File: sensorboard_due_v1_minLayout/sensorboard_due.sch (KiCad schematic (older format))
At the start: 35 parts, among them J1 LED_PANEL, J10 DHT22, J11 DHT2_JUMP, J12 DHT4_JUMP, J13 DHT22, J14 DHT22, J2 I2C_SLAVE, J3 WATCHDOG, J4 GPS_UBLOX_NEO6M, J5 GPS_DIS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

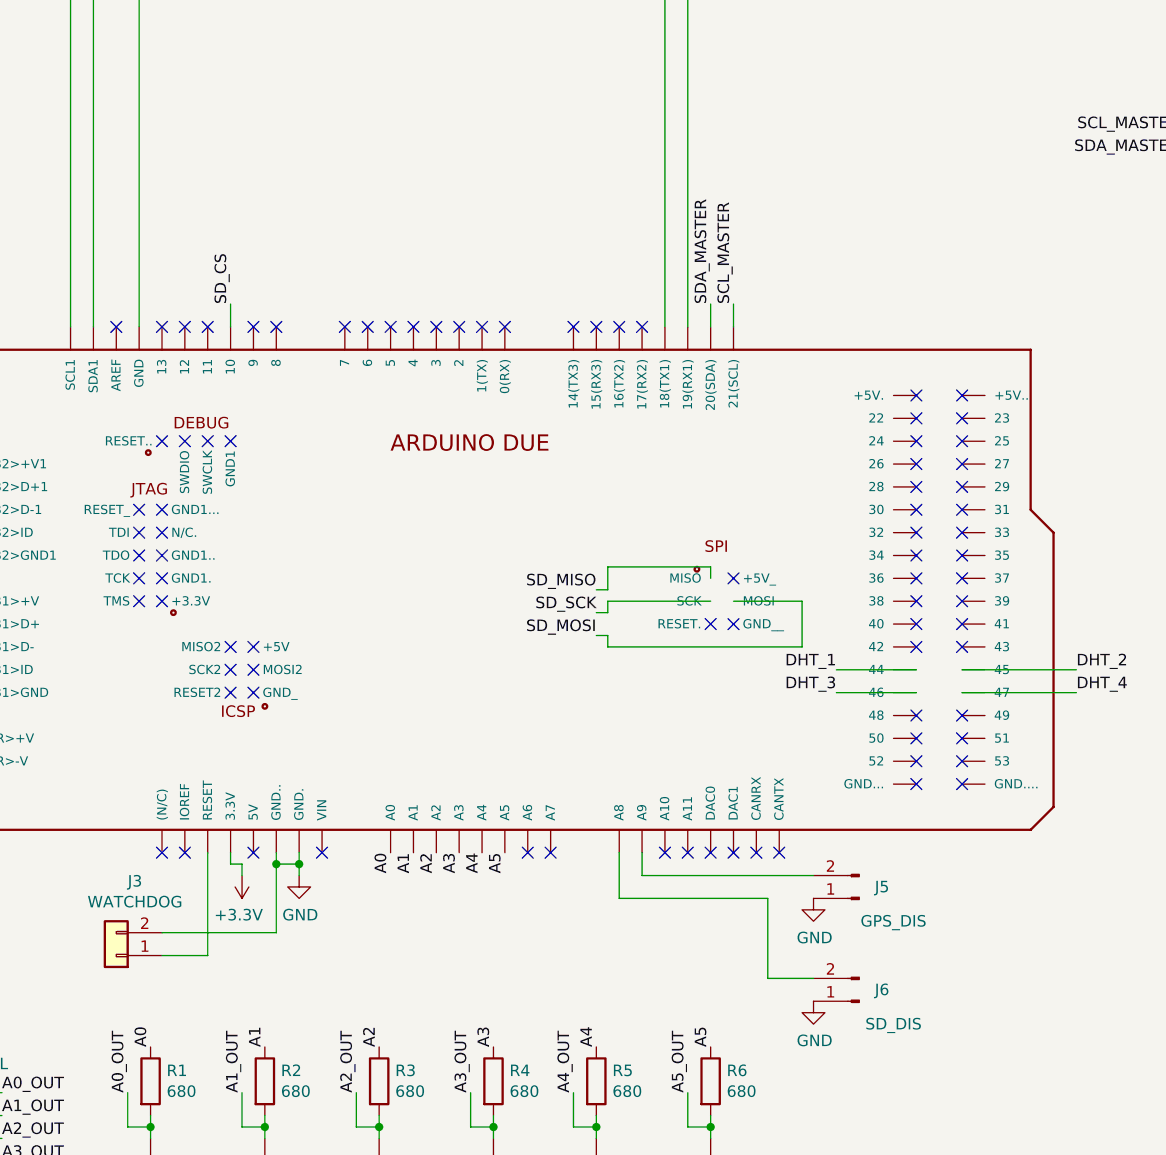
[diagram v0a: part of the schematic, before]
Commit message: pcb footprints for breadboard components should be accurate to datasheet (callipers if no ds) now
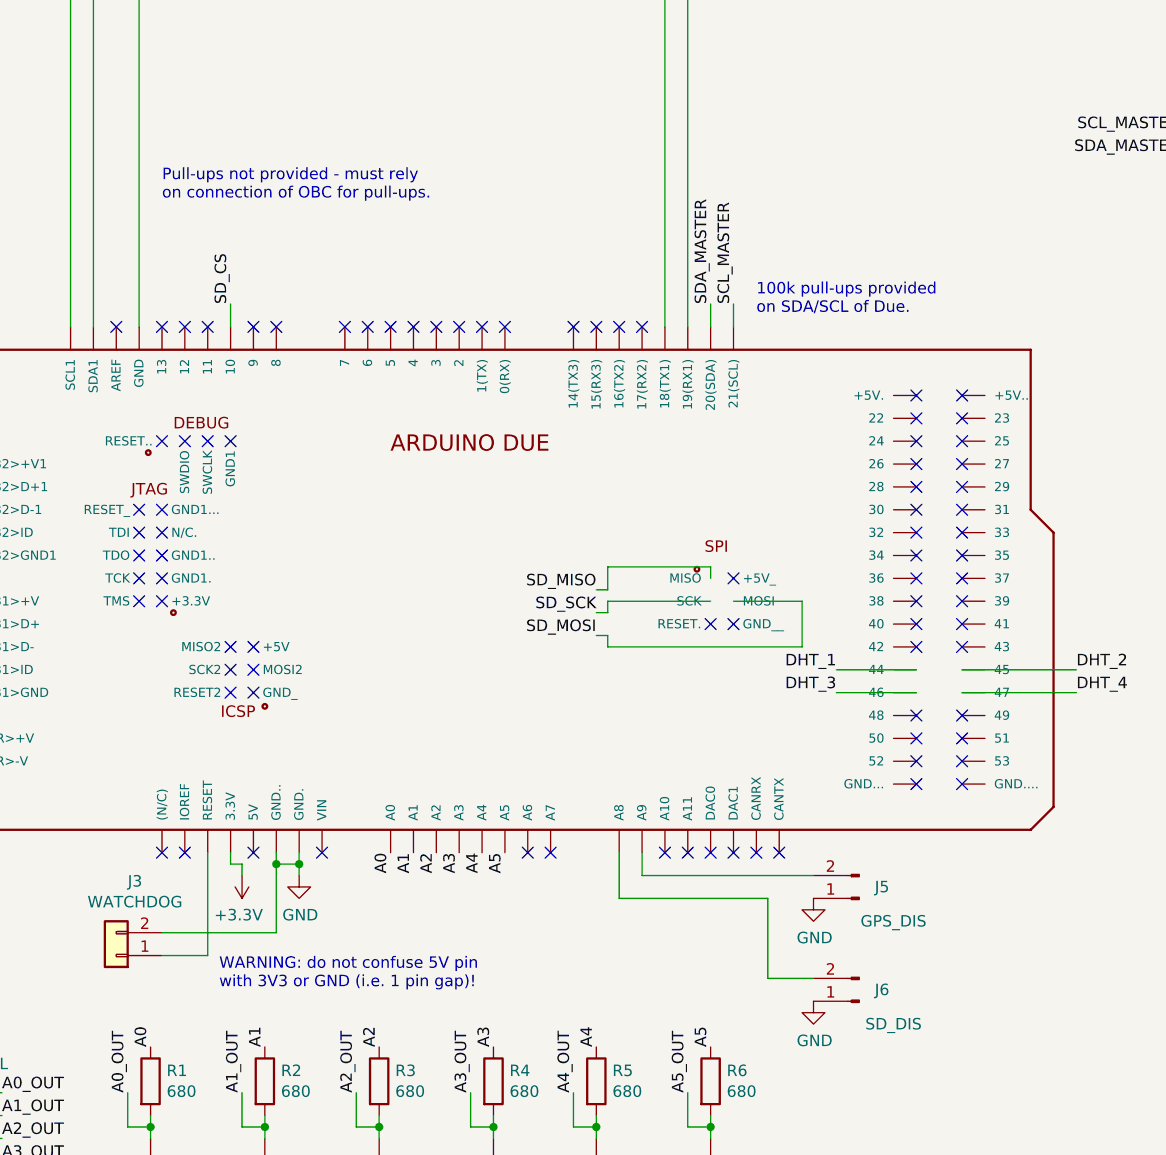
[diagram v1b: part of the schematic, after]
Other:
- note added: "100k pull-ups provided\non SDA/SCL of Due."
- note added: "Pull-ups not provided - must rely\non connection of OBC for pull-ups."
- note added: "WARNING: do not confuse 5V pin\nwith 3V3 or GND (i.e. 1 pin gap)!"
